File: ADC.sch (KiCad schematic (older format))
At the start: 4 parts

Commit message: Many additions; the system's almost together.  Just need to tidy up a few things around the PSU and the input stage.
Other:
- note added: "TODO:\nInput stage:\n * Roofing filter\n * Generally all component values\nPSU Internal:\n * Investigate PSRR of PCM4222 to see if the Sulzers are even required.\n * Determine feedback cap value\n * Confirm selection of pass transistors\n * Heatsinking of regs and trans?\n"
- note removed: "TODO:\nInput stage:\n * Roofing filter\n * Generally all component values\nPSU:\n * -15 V\n * +4 V\n * Investigate PSRR of PCM4222 to see if the Sulzers are even required.\n"
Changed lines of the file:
@@
 LIBS:my-conn
 LIBS:ADC-cache
-EELAYER 27 0
+EELAYER 24 0
 EELAYER END
 $Descr A4 11693 8268
@@
 Wire Wire Line
 	3300 4050 3600 4050
-Text Notes 950  1200 0    60   ~ 0
-TODO:\nInput stage:\n  * Roofing filter\n  * Generally all component values\nPSU:\n  * -15 V\n  * +4 V\n  * Investigate PSRR of PCM4222 to see if the Sulzers are even required.\n
+Text Notes 1000 2050 0    60   ~ 0
+TODO:\nInput stage:\n  * Roofing filter\n  * Generally all component values\nPSU Internal:\n  * Investigate PSRR of PCM4222 to see if the Sulzers are even required.\n  * Determine feedback cap value\n  * Confirm selection of pass transistors\n  * Heatsinking of regs and trans?\n
 $EndSCHEMATC

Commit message: First complete system.  Still a few things to check.
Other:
- note added: "TODO:\nPSU Internal:\n * Determine feedback cap value\n * Confirm selection of pass transistors\n * Heatsinking of regs and trans?\nOverall:\n * Signal path R and noise, loading on final stage by PCM4222EVM"
- note removed: "TODO:\nInput stage:\n * Roofing filter\n * Generally all component values\nPSU Internal:\n * Investigate PSRR of PCM4222 to see if the Sulzers are even required.\n * Determine feedback cap value\n * Confirm selection of pass transistors\n * Heatsinking of regs and trans?\n"
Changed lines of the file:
@@
 LIBS:my-conn
 LIBS:ADC-cache
-EELAYER 24 0
+EELAYER 27 0
 EELAYER END
 $Descr A4 11693 8268
@@
 Sheet 1 6
 Title ""
-Date "12 may 2014"
+Date "21 may 2014"
 Rev ""
 Comp ""
@@
 	3300 4050 3600 4050
 Text Notes 1000 2050 0    60   ~ 0
-TODO:\nInput stage:\n  * Roofing filter\n  * Generally all component values\nPSU Internal:\n  * Investigate PSRR of PCM4222 to see if the Sulzers are even required.\n  * Determine feedback cap value\n  * Confirm selection of pass transistors\n  * Heatsinking of regs and trans?\n
+TODO:\nPSU Internal:\n  * Determine feedback cap value\n  * Confirm selection of pass transistors\n  * Heatsinking of regs and trans?\nOverall:\n  * Signal path R and noise, loading on final stage by PCM4222EVM
 $EndSCHEMATC

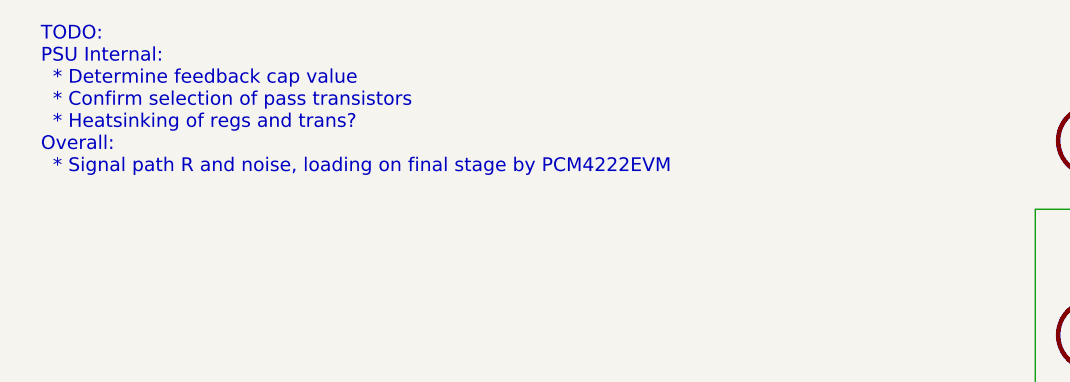
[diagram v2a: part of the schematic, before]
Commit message: Noise analysis completed; signal section finished.
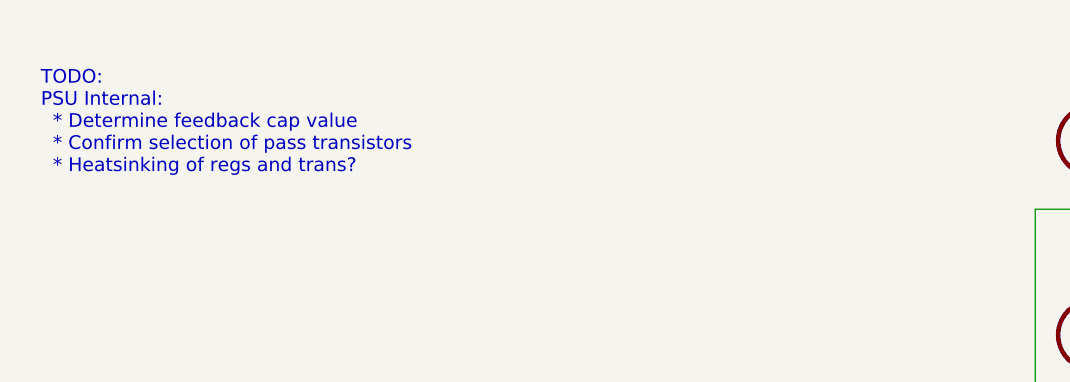
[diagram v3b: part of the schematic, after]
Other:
- note added: "TODO:\nPSU Internal:\n * Determine feedback cap value\n * Confirm selection of pass transistors\n * Heatsinking of regs and trans?\n"
- note removed: "TODO:\nPSU Internal:\n * Determine feedback cap value\n * Confirm selection of pass transistors\n * Heatsinking of regs and trans?\nOverall:\n * Signal path R and noise, loading on final stage by PCM4222EVM"
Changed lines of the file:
@@
 	3300 4050 3600 4050
 Text Notes 1000 2050 0    60   ~ 0
-TODO:\nPSU Internal:\n  * Determine feedback cap value\n  * Confirm selection of pass transistors\n  * Heatsinking of regs and trans?\nOverall:\n  * Signal path R and noise, loading on final stage by PCM4222EVM
+TODO:\nPSU Internal:\n  * Determine feedback cap value\n  * Confirm selection of pass transistors\n  * Heatsinking of regs and trans?\n
 $EndSCHEMATC

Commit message: V1.0 Schematic Completed.
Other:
- note removed: "TODO:\nPSU Internal:\n * Determine feedback cap value\n * Confirm selection of pass transistors\n * Heatsinking of regs and trans?\n"
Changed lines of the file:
@@
 Wire Wire Line
 	3300 4050 3600 4050
-Text Notes 1000 2050 0    60   ~ 0
-TODO:\nPSU Internal:\n  * Determine feedback cap value\n  * Confirm selection of pass transistors\n  * Heatsinking of regs and trans?\n
 $EndSCHEMATC

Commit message: Added component numbers.
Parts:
- gave numbers to parts that had none: 4
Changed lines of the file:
@@
 $EndSheet
 $Comp
-L CONN_6 P?
+L CONN_6 P1
 U 1 1 5368BA3A
 P 2500 4550
-F 0 "P?" V 2450 4550 60  0000 C CNN
+F 0 "P1" V 2450 4550 60  0000 C CNN
 F 1 "CONN_6" V 2550 4550 60  0000 C CNN
 F 2 "" H 2500 4550 60  0000 C CNN
@@
 $EndComp
 $Comp
-L CONN_6 P?
+L CONN_6 P2
 U 1 1 5368BCA4
 P 2900 4550
-F 0 "P?" V 2850 4550 60  0000 C CNN
+F 0 "P2" V 2850 4550 60  0000 C CNN
 F 1 "CONN_6" V 2950 4550 60  0000 C CNN
 F 2 "" H 2900 4550 60  0000 C CNN
@@
 $EndSheet
 $Comp
-L RCA J?
+L RCA J1
 U 1 1 536ED27A
 P 5600 1900
-F 0 "J?" H 5850 1750 60  0000 L CNN
+F 0 "J1" H 5850 1750 60  0000 L CNN
 F 1 "RCA" H 5850 1650 60  0000 L CNN
 F 2 "" H 5600 1900 60  0000 C CNN
@@
 $EndComp
 $Comp
-L RCA J?
+L RCA J2
 U 1 1 536ED287
 P 5600 2750
-F 0 "J?" H 5850 2600 60  0000 L CNN
+F 0 "J2" H 5850 2600 60  0000 L CNN
 F 1 "RCA" H 5850 2500 60  0000 L CNN
 F 2 "" H 5600 2750 60  0000 C CNN

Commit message: More components specified
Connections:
- no-connect marks 0 -> 1
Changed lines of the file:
@@
 Sheet 1 6
 Title ""
-Date "23 may 2014"
+Date "25 may 2014"
 Rev ""
 Comp ""
@@
 Wire Wire Line
 	3300 4050 3600 4050
+NoConn ~ 3250 4300
 $EndSCHEMATC
